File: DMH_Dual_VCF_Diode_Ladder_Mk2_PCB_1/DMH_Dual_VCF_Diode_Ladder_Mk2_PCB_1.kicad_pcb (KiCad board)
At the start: 2 copper layers, 146 x 175 mm, 226 parts, among them J0 Conn_01x01, J1 TS_Jack_6.35mm_Sw, J10 TS_Jack_6.35mm_Sw, J100 IDC_02x08, J11 TS_Jack_6.35mm_Sw, J12 TS_Jack_6.35mm_Sw, J13 TS_Jack_6.35mm_Sw, J14 TS_Jack_6.35mm_Sw, J15 Conn_01x08_PinHeader, J16 Conn_01x08_PinHeader, J17 Conn_01x06_PinHeader, J18 Conn_01x06_PinHeader, J19 Conn_01x04_PinHeader, J2 TS_Jack_6.35mm_Sw, J20 Conn_01x04_PinHeader, J200 IDC_02x05, J21 Conn_01x06_PinHeader, J210 IDC_02x05, J22 Conn_01x06_PinHeader, J23 Conn_01x04_PinHeader, J3 TS_Jack_6.35mm_Sw, J4 TS_Jack_6.35mm_Sw, J5 TS_Jack_6.35mm_Sw, J6 TS_Jack_6.35mm_Sw, J7 TS_Jack_6.35mm_Sw, J8 TS_Jack_6.35mm_Sw, J9 TS_Jack_6.35mm_Sw, Q1 BC548, Q2 BC548, Q3 BC548, Q4 BC548, Q5 BC548, Q6 BC548, Q7 BC548, Q8 BC548, U1 TL074, U10 TL074, U2 TL074, U3 TL074, U4 TL074, U5 TL074, U6 TL074, U7 TL074, U8 TL074, U9 TL074

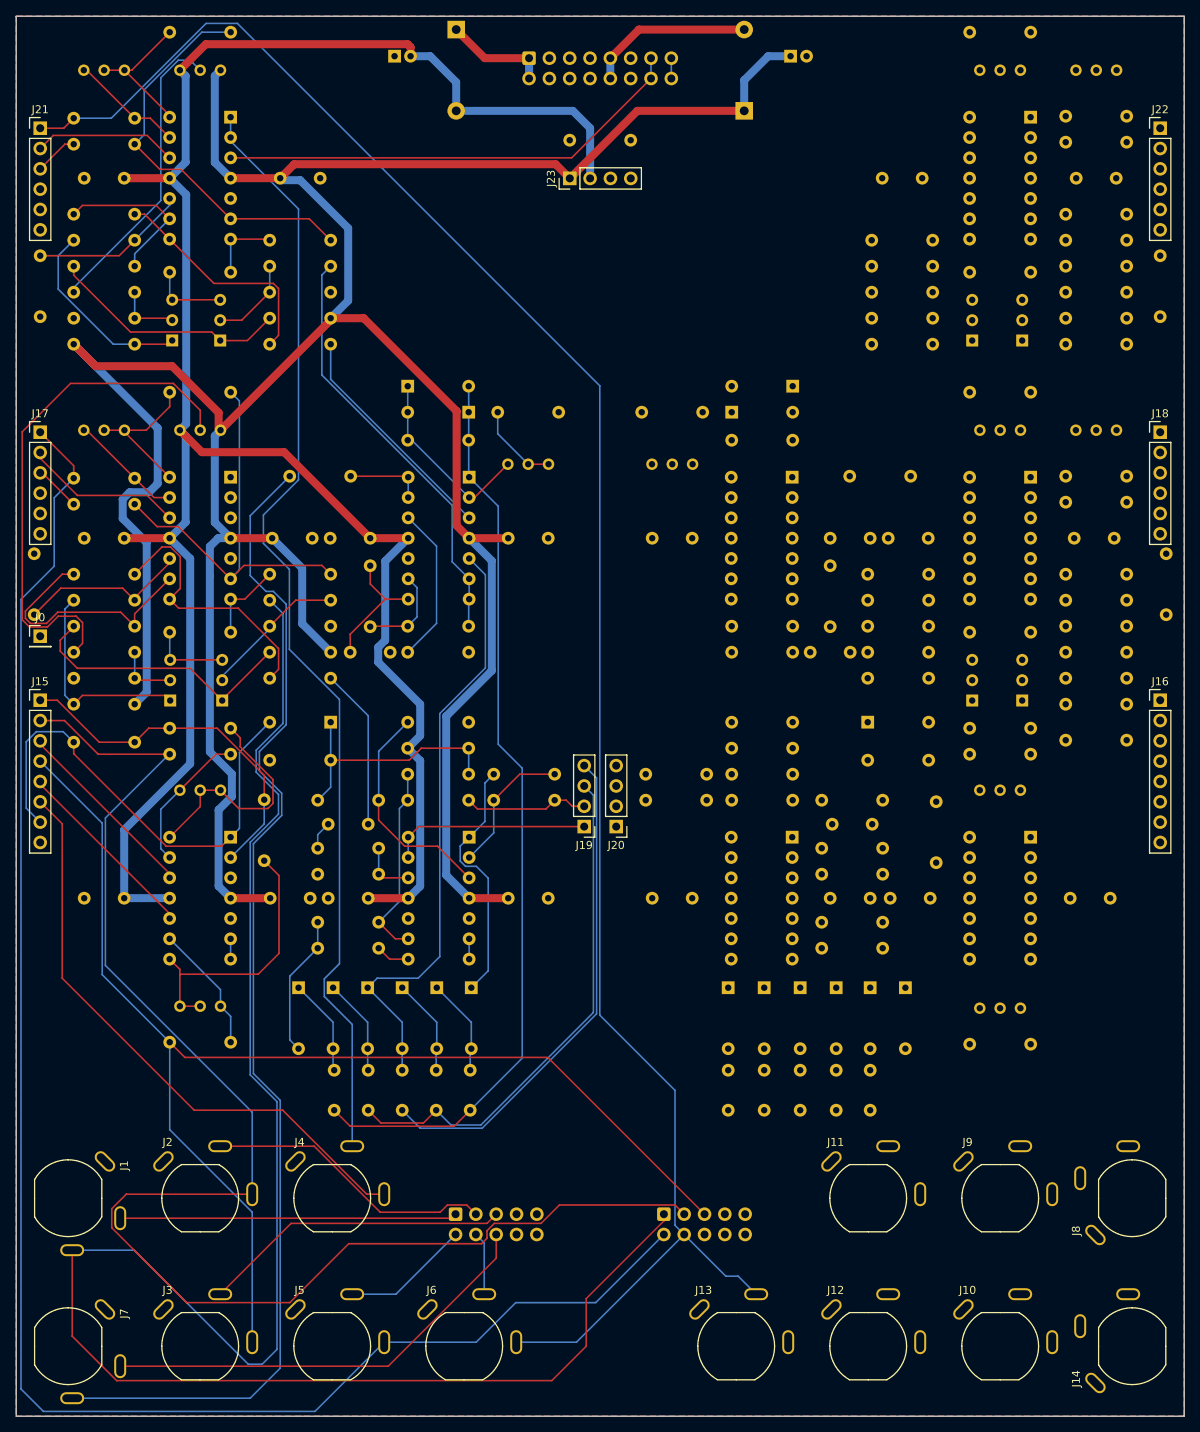
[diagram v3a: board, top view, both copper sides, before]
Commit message: Routed circuit B
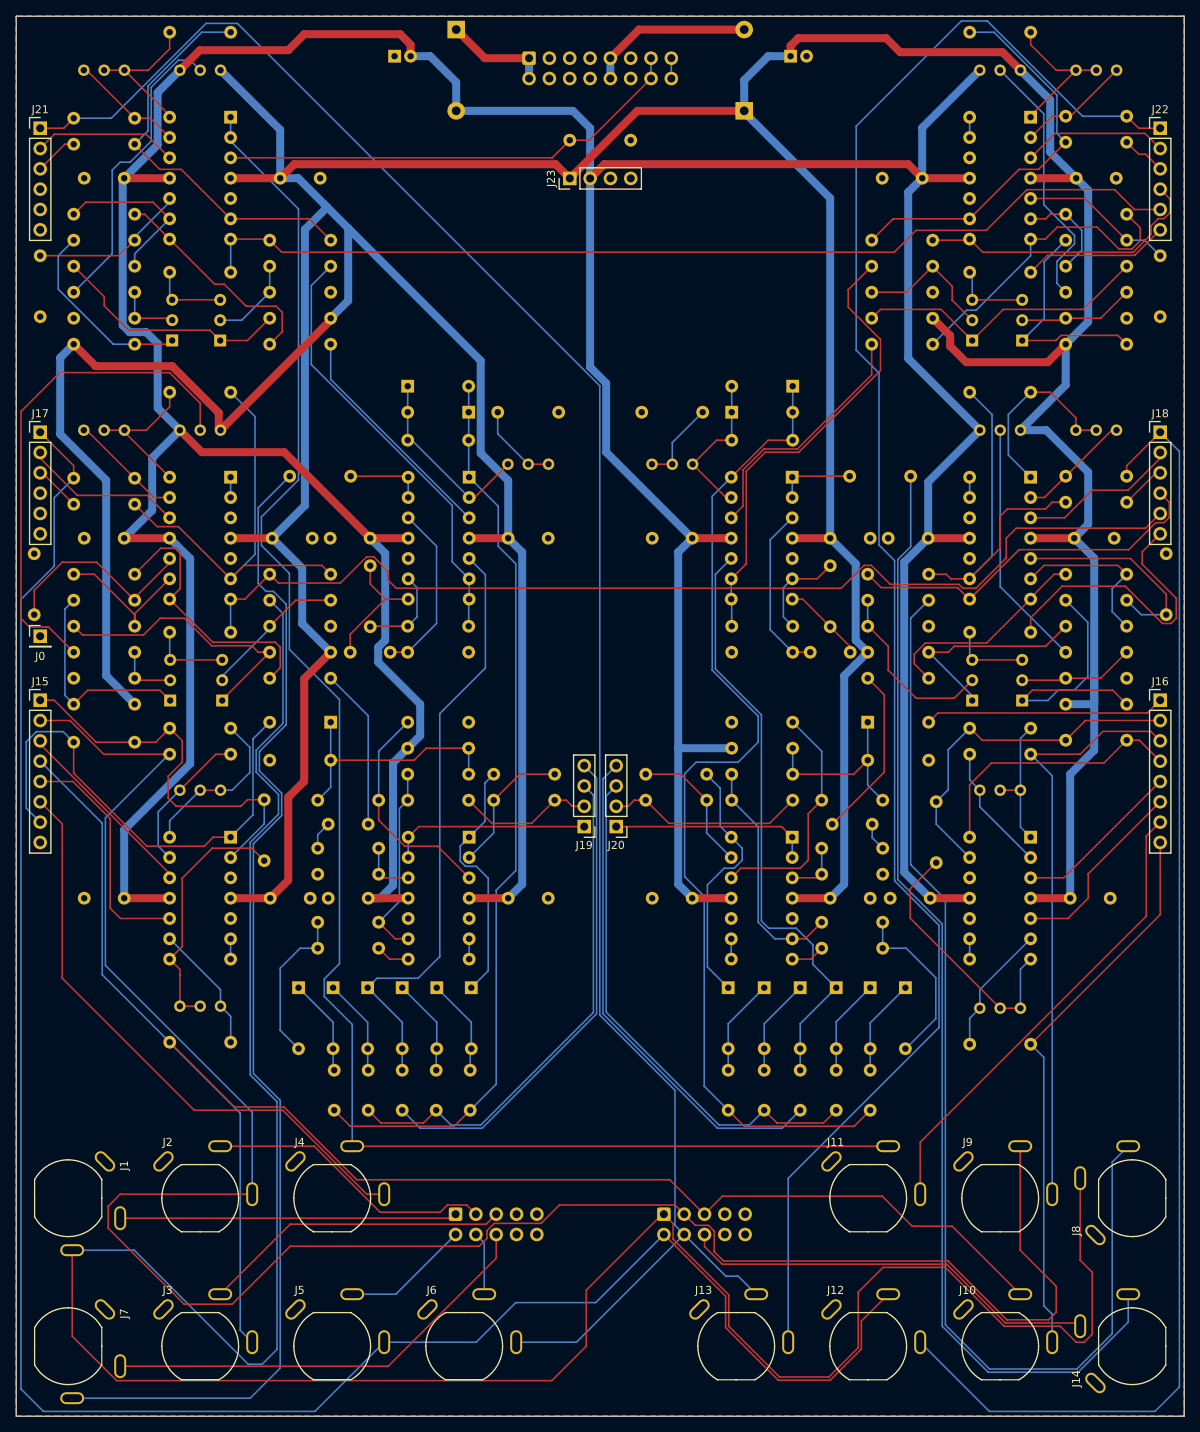
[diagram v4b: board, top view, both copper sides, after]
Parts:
- moved R124 7.62 mm to (158.2, 122.0), turned to 0 degrees
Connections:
- J16 pad 1: Net-(J16A-Pin_1) -> /CV Processing/Link CV Switch
- J16 pad 2: /CV Processing/CV1 B Input -> Net-(J16B-Pin_2)
- J16 pad 3: Net-(J16C-Pin_3) -> /CV Processing/CV1 B Input
- J16 pad 4: /CV Processing/CV2 B Input -> /CV Processing/CV B
- J16 pad 6: /CV Processing/CV3 B Input -> Net-(J16F-Pin_6)
- J16 pad 7: /CV Processing/CV B -> /CV Processing/CV3 B Input
- J16 pad 8: /CV Processing/Link CV Switch -> /CV Processing/CV2 B Input
- R19 pad 2: Net-(J16A-Pin_1) -> Net-(J16B-Pin_2)
- R20 pad 1: Net-(J16A-Pin_1) -> Net-(J16B-Pin_2)
- R22 pad 2: Net-(J16A-Pin_1) -> Net-(J16B-Pin_2)
- U8 pad 13: Net-(J16A-Pin_1) -> Net-(J16B-Pin_2)
- U8 pad 3: Net-(J16C-Pin_3) -> Net-(J16E-Pin_5)
- U8 pad 5: Net-(J16E-Pin_5) -> Net-(J16F-Pin_6)
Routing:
- net +12V: track 404.0 -> 732.9 mm
- net -12V: track 284.3 -> 581.7 mm
- net /Inputs and Outputs B/Res CV Jack: track 0.00 -> 213.1 mm
- net /Drive B/Drive CV Input: track 0.00 -> 164.8 mm
- net /Drive B/Input: track 0.00 -> 142.5 mm
- net /Core Circuit B/Output: track 0.00 -> 140.9 mm
- net Net-(D22-A): track 0.00 -> 127.4 mm
- net /Drive A/Drive CV: track 10.3 -> 133.4 mm
- net /Resonance A CV/Res CV: track 9.09 -> 125.3 mm
- net /Drive A/Input: track 231.6 -> 331.3 mm
- net /CV Processing/CV1 A Input: track 186.1 -> 263.9 mm
- net Net-(D18-K): track 0.00 -> 74.9 mm
- net /CV Processing/CV1 B Input: track 0.00 -> 74.0 mm
- net /CV Processing/CV2 B Input: track 0.00 -> 70.3 mm
- net /Inputs and Outputs A/CV 3 TN: track 140.1 -> 207.3 mm
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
